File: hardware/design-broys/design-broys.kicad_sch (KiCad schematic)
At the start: 2 parts, among them U1 ESP32-C3FH4, U2 W25Q16JVSSIQ

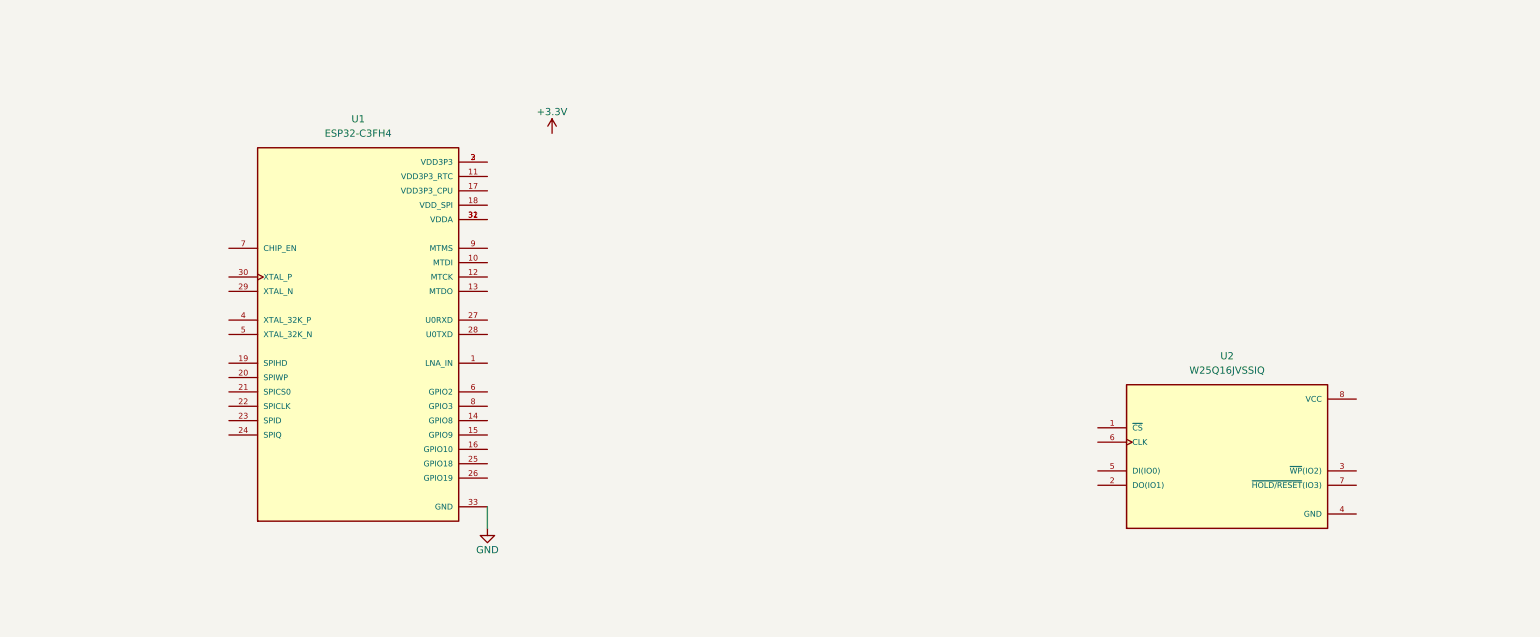
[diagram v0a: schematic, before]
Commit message: Fixed the issue with kicad versioning
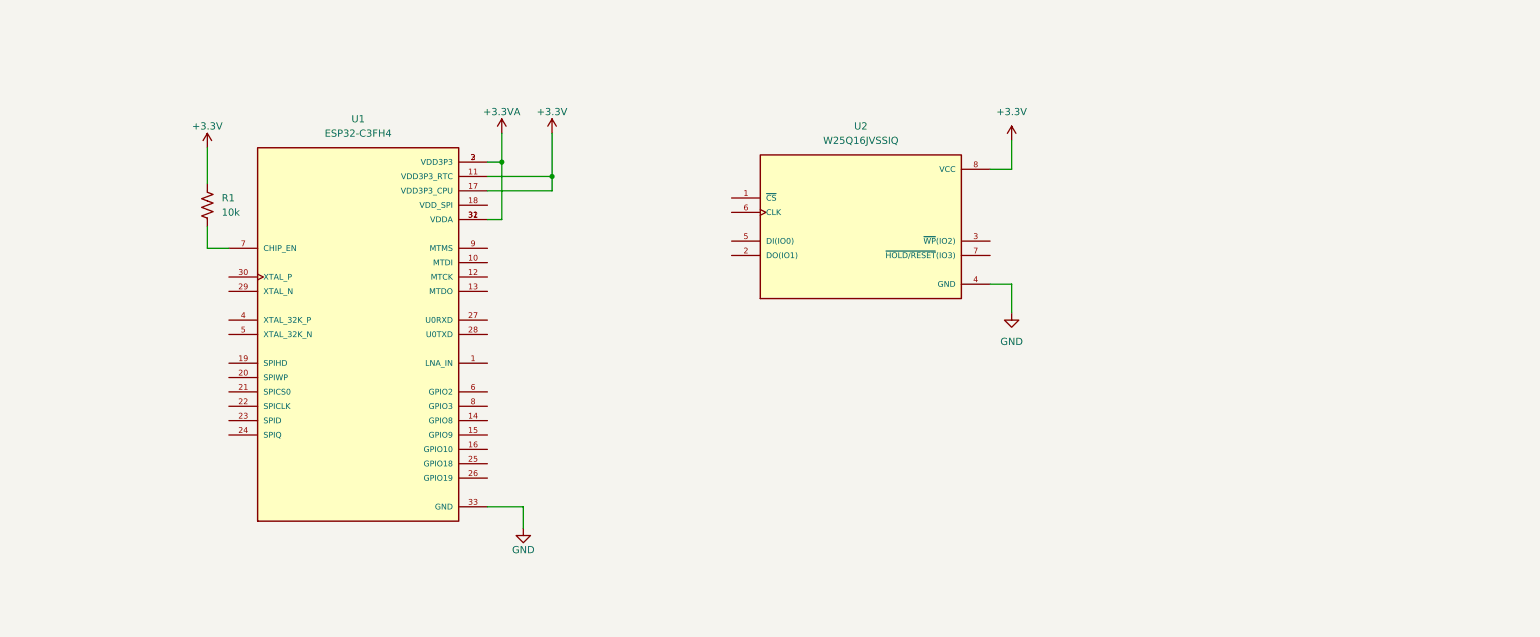
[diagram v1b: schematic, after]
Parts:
- added R1: 10k, Resistor_SMD:R_0402_1005Metric, symbol Device:R_US
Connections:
- net +3V3: now also U1.11 (VDD3P3_RTC), U1.17 (VDD3P3_CPU), U2.8 (VCC), R1.1
- net GND: now also U2.4 (GND)
- net +3.3VA: now reaches U1.2 (VDD3P3), U1.3 (VDD3P3)
- net +3.3VA: now also U1.31 (VDDA), U1.32 (VDDA)
- net at U1.7 (CHIP_EN): now also R1.2
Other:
- moved on the sheet: U2

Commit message: Connected flash with the esp.
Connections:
- net CS-memory: now reaches U2.1 (~{CS})
- net CS-memory: now also U1.21 (SPICS0)
- net DO-memory: now reaches U2.2 (DO(IO1))
- net DO-memory: now also U1.24 (SPIQ)
- net DI-memory: now reaches U2.5 (DI(IO0))
- net DI-memory: now also U1.23 (SPID)
- net SPICLK-memory: now reaches U2.6 (CLK)
- net SPICLK-memory: now also U1.22 (SPICLK)
- no-connect marks 0 -> 2
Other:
- note added: "Flash memory"
- moved on the sheet: U2

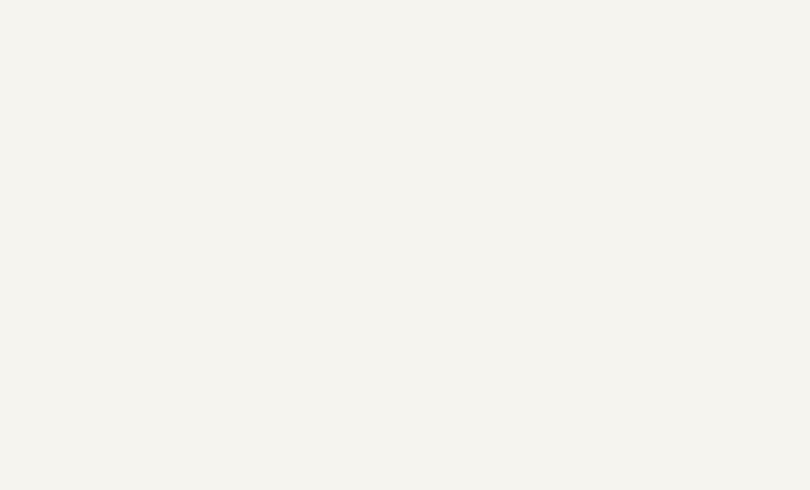
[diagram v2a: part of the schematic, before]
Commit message: Added LEDs for the first digit.
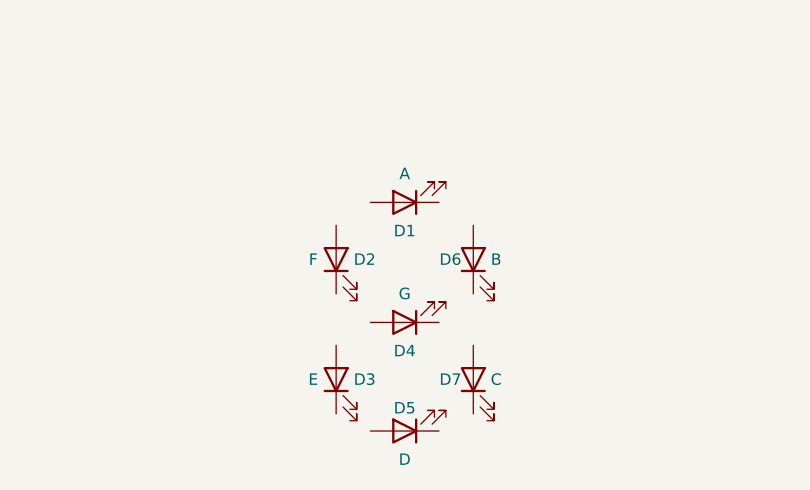
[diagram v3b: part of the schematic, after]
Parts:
- added D1: A, LED_SMD:LED_0603_1608Metric, symbol Device:LED
- added D2: F, LED_SMD:LED_0603_1608Metric, symbol Device:LED
- added D3: E, LED_SMD:LED_0603_1608Metric, symbol Device:LED
- added D4: G, LED_SMD:LED_0603_1608Metric, symbol Device:LED
- added D5: D, LED_SMD:LED_0603_1608Metric, symbol Device:LED
- added D6: B, LED_SMD:LED_0603_1608Metric, symbol Device:LED
- added D7: C, LED_SMD:LED_0603_1608Metric, symbol Device:LED
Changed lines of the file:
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@@
     (pin "1")
+  )
+  (symbol (lib_id "Device:LED") (at 147.32 112.395 90) (unit 1)
+    (in_bom yes) (on_board yes)
+    (property "Reference" "D3" (id 0) (at 150.495 112.395 90))
+    (property "Value" "E" (id 1) (at 144.78 112.395 90))
+    (property "Footprint" "LED_SMD:LED_0603_1608Metric" (id 2) (at 151.13 112.395 0)
+      (effects (font (size 1.27 1.27)) hide)
+    )
+    (property "Datasheet" "~" (id 3) (at 147.32 112.395 0)
+      (effects (font (size 1.27 1.27)) hide)
+    )
+    (pin "1")
+    (pin "2")
   )
   (symbol (lib_id "power:GND") (at 101.6 105.41 0) (unit 1)
@@
     )
     (pin "1")
+  )
+  (symbol (lib_id "Device:LED") (at 154.94 92.71 180) (unit 1)
+    (in_bom yes) (on_board yes)
+    (property "Reference" "D1" (id 0) (at 154.94 95.885 0))
+    (property "Value" "A" (id 1) (at 154.94 89.535 0))
+    (property "Footprint" "LED_SMD:LED_0603_1608Metric" (id 2) (at 154.94 88.9 0)
+      (effects (font (size 1.27 1.27)) hide)
+    )
+    (property "Datasheet" "~" (id 3) (at 154.94 92.71 0)
+      (effects (font (size 1.27 1.27)) hide)
+    )
+    (pin "1")
+    (pin "2")
+  )
+  (symbol (lib_id "Device:LED") (at 154.94 118.11 180) (unit 1)
+    (in_bom yes) (on_board yes)
+    (property "Reference" "D5" (id 0) (at 154.94 115.57 0))
+    (property "Value" "D" (id 1) (at 154.94 121.285 0))
+    (property "Footprint" "LED_SMD:LED_0603_1608Metric" (id 2) (at 154.94 114.3 0)
+      (effects (font (size 1.27 1.27)) hide)
+    )
+    (property "Datasheet" "~" (id 3) (at 154.94 118.11 0)
+      (effects (font (size 1.27 1.27)) hide)
+    )
+    (pin "1")
+    (pin "2")
+  )
+  (symbol (lib_id "Device:LED") (at 162.56 112.395 90) (unit 1)
+    (in_bom yes) (on_board yes)
+    (property "Reference" "D7" (id 0) (at 160.02 112.395 90))
+    (property "Value" "C" (id 1) (at 165.1 112.395 90))
+    (property "Footprint" "LED_SMD:LED_0603_1608Metric" (id 2) (at 166.37 112.395 0)
+      (effects (font (size 1.27 1.27)) hide)
+    )
+    (property "Datasheet" "~" (id 3) (at 162.56 112.395 0)
+      (effects (font (size 1.27 1.27)) hide)
+    )
+    (pin "1")
+    (pin "2")
   )
   (symbol (lib_id "power:+3.3VA") (at 97.79 35.56 0) (unit 1)
@@
     (pin "1")
   )
+  (symbol (lib_id "Device:LED") (at 154.94 106.045 180) (unit 1)
+    (in_bom yes) (on_board yes)
+    (property "Reference" "D4" (id 0) (at 154.94 109.22 0))
+    (property "Value" "G" (id 1) (at 154.94 102.87 0))
+    (property "Footprint" "LED_SMD:LED_0603_1608Metric" (id 2) (at 154.94 102.235 0)
+      (effects (font (size 1.27 1.27)) hide)
+    )
+    (property "Datasheet" "~" (id 3) (at 154.94 106.045 0)
+      (effects (font (size 1.27 1.27)) hide)
+    )
+    (pin "1")
+    (pin "2")
+  )
   (symbol (lib_id "power:+3.3V") (at 106.68 35.56 0) (unit 1)
     (in_bom yes) (on_board yes)
@@
     )
     (pin "1")
+  )
+  (symbol (lib_id "Device:LED") (at 147.32 99.06 90) (unit 1)
+    (in_bom yes) (on_board yes)
+    (property "Reference" "D2" (id 0) (at 150.495 99.06 90))
+    (property "Value" "F" (id 1) (at 144.78 99.06 90))
+    (property "Footprint" "LED_SMD:LED_0603_1608Metric" (id 2) (at 151.13 99.06 0)
+      (effects (font (size 1.27 1.27)) hide)
+    )
+    (property "Datasheet" "~" (id 3) (at 147.32 99.06 0)
+      (effects (font (size 1.27 1.27)) hide)
+    )
+    (pin "1")
+    (pin "2")
   )
   (symbol (lib_id "W25Q16JVSSIQ:W25Q16JVSSIQ") (at 251.46 36.83 0) (unit 1)
@@
     (pin "7")
     (pin "8")
+  )
+  (symbol (lib_id "Device:LED") (at 162.56 99.06 90) (unit 1)
+    (in_bom yes) (on_board yes)
+    (property "Reference" "D6" (id 0) (at 160.02 99.06 90))
+    (property "Value" "B" (id 1) (at 165.1 99.06 90))
+    (property "Footprint" "LED_SMD:LED_0603_1608Metric" (id 2) (at 166.37 99.06 0)
+      (effects (font (size 1.27 1.27)) hide)
+    )
+    (property "Datasheet" "~" (id 3) (at 162.56 99.06 0)
+      (effects (font (size 1.27 1.27)) hide)
+    )
+    (pin "1")
+    (pin "2")
   )
   (symbol (lib_id "power:+3.3V") (at 45.72 38.1 0) (unit 1)
@@
       (reference "#PWR06") (unit 1) (value "GND") (footprint "")
     )
+    (path "/2a85eac6-ce98-4719-81e9-43d8fbb9d534"
+      (reference "D1") (unit 1) (value "A") (footprint "LED_SMD:LED_0603_1608Metric")
+    )
+    (path "/bf0a2e60-d1d9-4973-8982-c8d4bd0aad81"
+      (reference "D2") (unit 1) (value "F") (footprint "LED_SMD:LED_0603_1608Metric")
+    )
+    (path "/1d1344a6-0a2f-4255-82e4-767eff7e5340"
+      (reference "D3") (unit 1) (value "E") (footprint "LED_SMD:LED_0603_1608Metric")
+    )
+    (path "/91eb8c4c-d116-4493-86df-7a9ad44d93b6"
+      (reference "D4") (unit 1) (value "G") (footprint "LED_SMD:LED_0603_1608Metric")
+    )
+    (path "/3d757904-bbc0-44ac-9fdc-d7d2a233a6a2"
+      (reference "D5") (unit 1) (value "D") (footprint "LED_SMD:LED_0603_1608Metric")
+    )
+    (path "/d2ff522f-268e-4842-bcf1-d3453ef8cc87"
+      (reference "D6") (unit 1) (value "B") (footprint "LED_SMD:LED_0603_1608Metric")
+    )
+    (path "/4bf8578e-0f94-42e2-8200-19add73147d0"
+      (reference "D7") (unit 1) (value "C") (footprint "LED_SMD:LED_0603_1608Metric")
+    )
     (path "/e238c8f6-f81c-451c-b083-2e5d79bf81d5"
